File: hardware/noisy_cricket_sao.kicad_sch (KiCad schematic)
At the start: 30 parts, among them J1 SAO 6-Pin, U1 AD8107, U2 CH32V003F4U6

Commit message: Update low pass filter on schematic
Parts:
- removed C1-ALT1: 130pF, Capacitor_SMD:C_0402_1005Metric, symbol Device:C
- removed C2-ALT1: 8.66k, Resistor_SMD:R_0402_1005Metric, symbol Device:R_US
- removed C4: 1.3nF, Capacitor_SMD:C_0402_1005Metric, symbol Device:C
- removed R1: 26.1k, Resistor_SMD:R_0402_1005Metric, symbol Device:R_US
- removed R3-ALT1: 1uF, Capacitor_SMD:C_0402_1005Metric, symbol Device:C
- removed R4-ALT1: 52.3k, Resistor_SMD:R_0402_1005Metric, symbol Device:R_US
- C3: value 390nF -> 22nF
- C6: value 1uF -> 10uF; footprint Capacitor_SMD:C_0402_1005Metric -> Capacitor_SMD:C_0603_1608Metric
- R3: value 40.2 -> 750
- R5: value 100 -> 200
- R6, R7: value 0 -> 100
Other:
- note removed: "DNP and alternate parts are for multiple-feedback filter topology."
- note removed: "DNP-ALT"
- moved on the sheet: C2, C3, R3

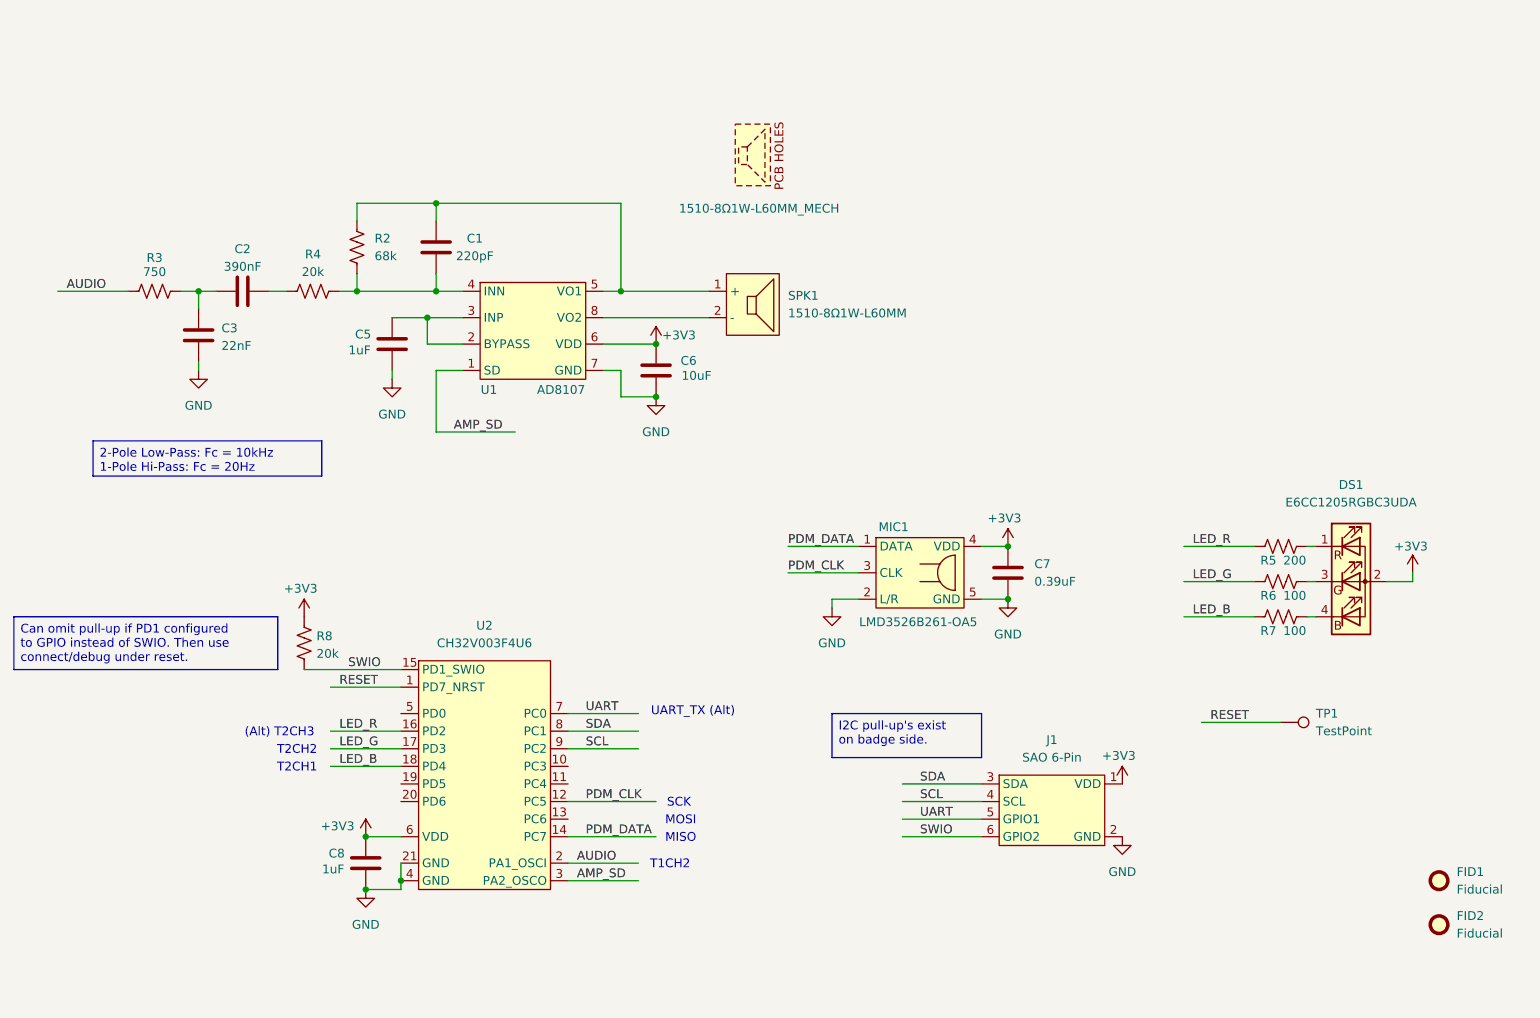
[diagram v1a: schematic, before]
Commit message: Switch to MSPM0
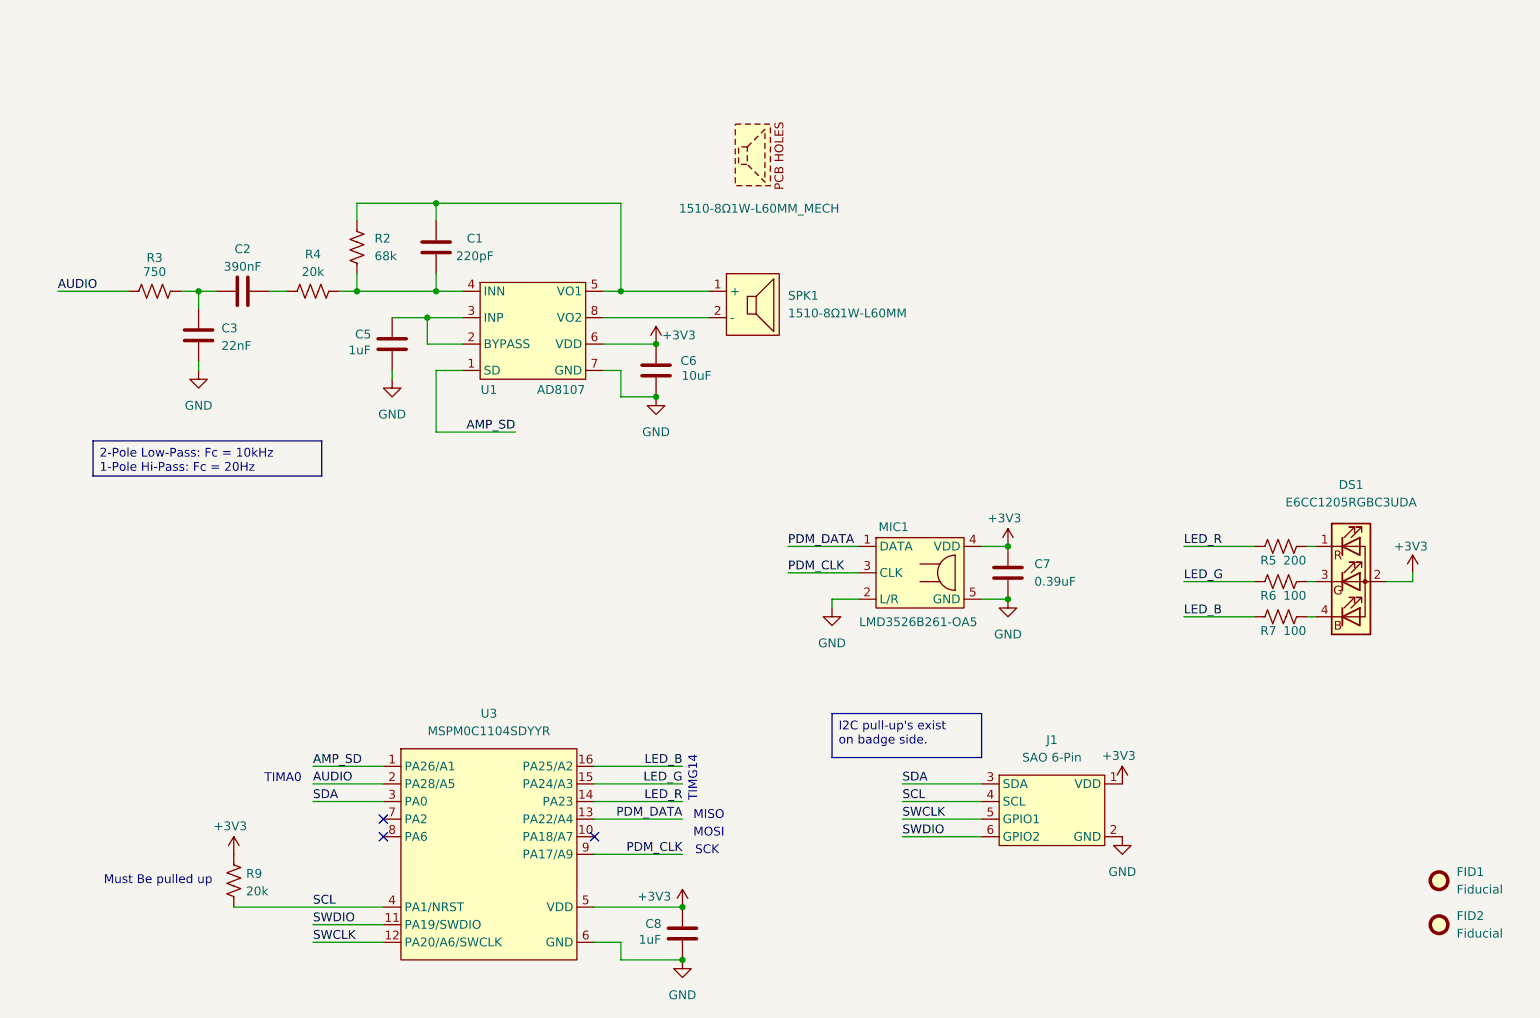
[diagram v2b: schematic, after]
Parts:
- removed R8: 20k, Resistor_SMD:R_0402_1005Metric, symbol Device:R_US
- removed TP1: TestPoint, TestPoint:TestPoint_Pad_D1.0mm, symbol Connector:TestPoint
- removed U2: CH32V003F4U6, noisy_cricket_sao:CH32V003F4U6, symbol noisy_cricket_sao:CH32V003F4U6
- added R9: 20k, Resistor_SMD:R_0402_1005Metric, symbol Device:R_US
- added U3: MSPM0C1104SDYYR, noisy_cricket_sao:SOT23-16-TI, symbol noisy_cricket_sao:MSPM0C1104SDYYR
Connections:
- net +3V3: now also R9.1, U3.5 (VDD)
- net AMP_SD: now also U3.1 (PA26/A1)
- net AUDIO: now also U3.2 (PA28/A5)
- net GND: now also U3.6 (GND)
- net LED_B: now also U3.16 (PA25/A2)
- net LED_G: now also U3.15 (PA24/A3)
- net LED_R: now also U3.14 (PA23)
- net PDM_CLK: now also U3.9 (PA17/A9)
- net PDM_DATA: now also U3.13 (PA22/A4)
- net SCL: now also R9.2, U3.4 (PA1/NRST)
- net SDA: now also U3.3 (PA0)
- net SWIO renamed SWDIO
- net SWDIO: now also U3.11 (PA19/SWDIO)
- net UART renamed SWCLK
- net SWCLK: now also U3.12 (PA20/A6/SWCLK)
- no-connect marks 0 -> 3
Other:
- note added: "Must Be pulled up"
- note added: "TIMA0"
- note added: "TIMG14"
- note removed: "(Alt) T2CH3"
- note removed: "T1CH2"
- note removed: "T2CH1"
- note removed: "T2CH2"
- note removed: "UART_TX (Alt)"
- moved on the sheet: C8
